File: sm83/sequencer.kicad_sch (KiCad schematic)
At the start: 62 parts

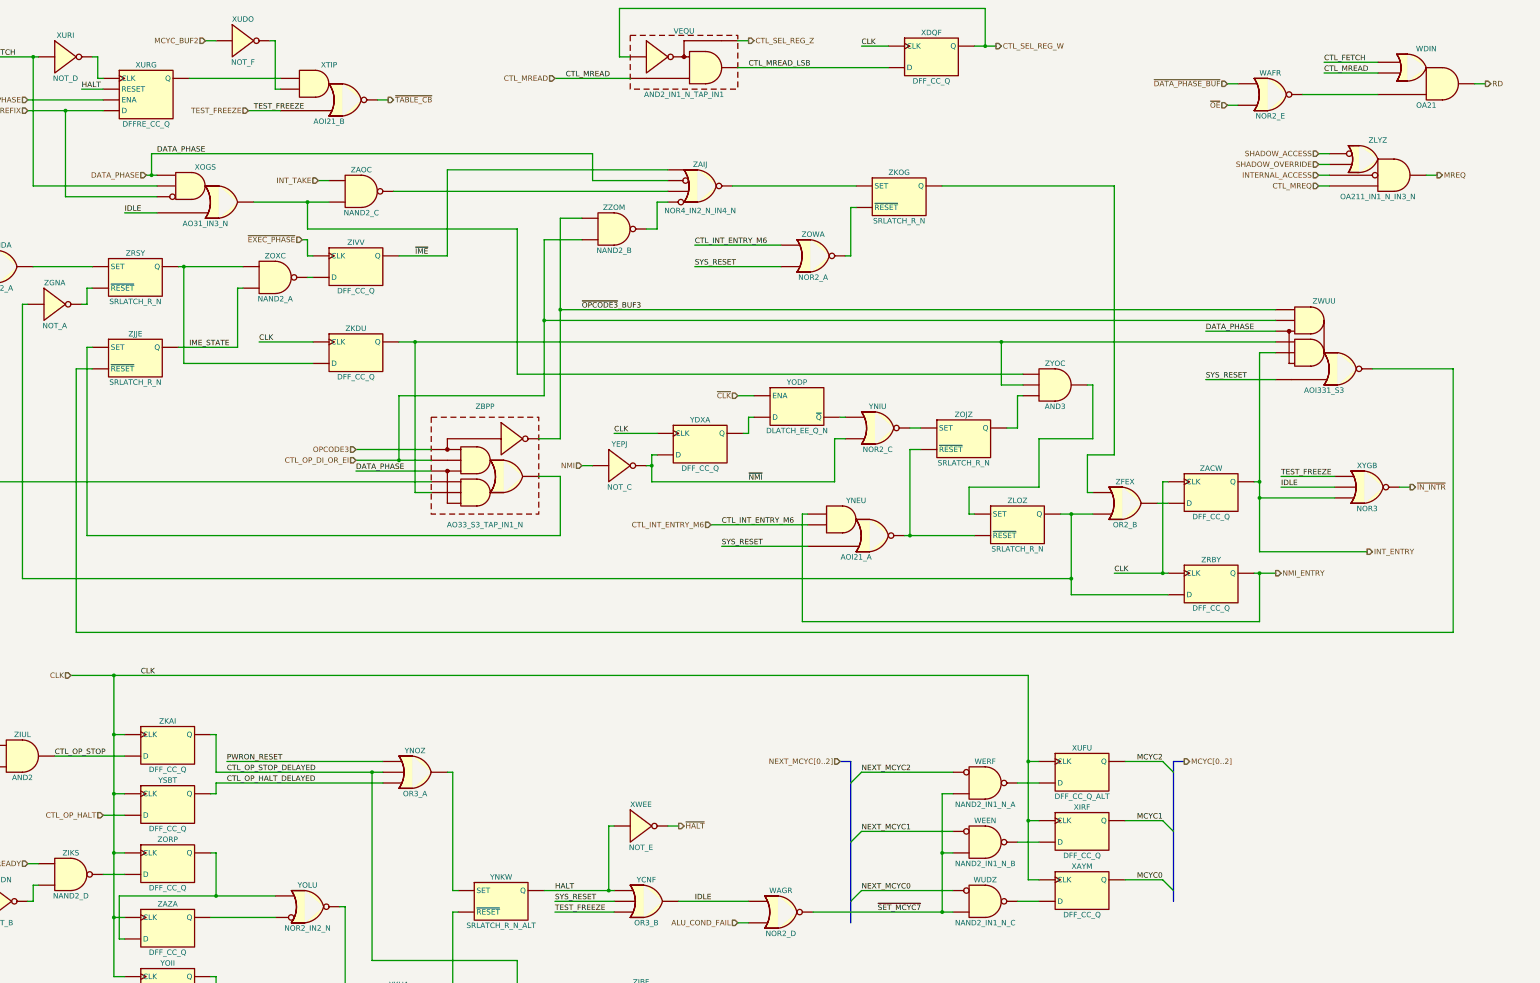
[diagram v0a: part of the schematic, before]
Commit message: SM83: Add decoder1 schematic
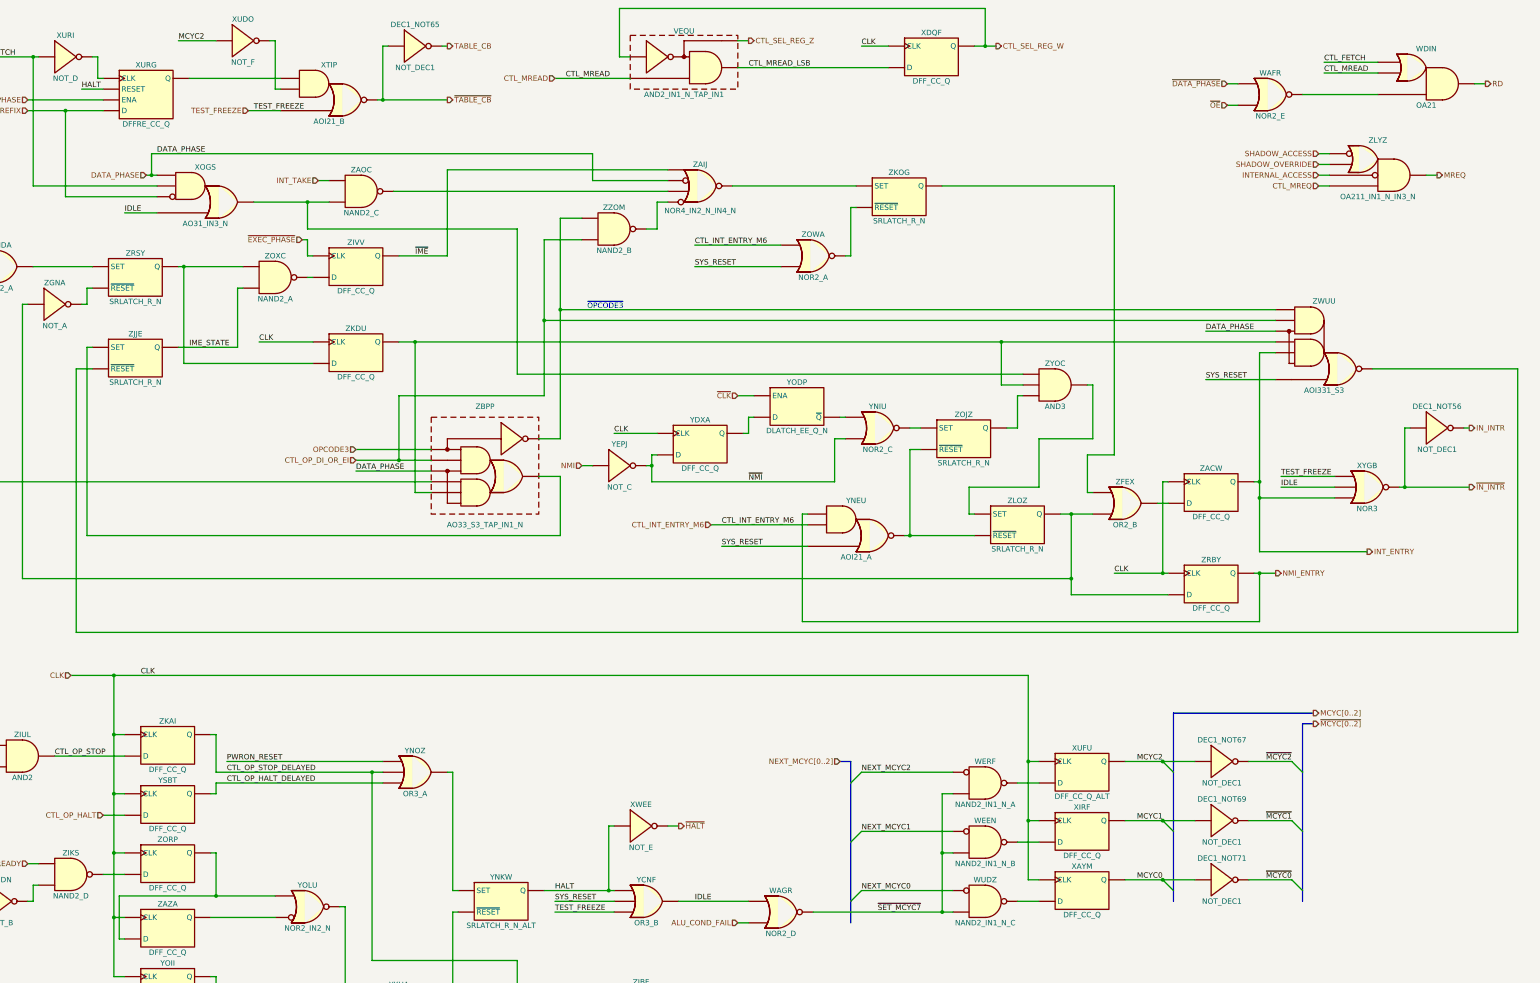
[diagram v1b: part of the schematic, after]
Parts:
- added DEC1_NOT56, DEC1_NOT65, DEC1_NOT67, DEC1_NOT69, DEC1_NOT71: NOT_DEC1, symbol SM83_Cells:NOT_DEC1
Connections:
- net MCYC_BUF2 is gone; now on net MCYC2: XUDO.1
- net MCYC0: now also DEC1_NOT71.1
- net MCYC1: now also DEC1_NOT69.1
- net MCYC2: now also DEC1_NOT67.1
- net ~{IN_INTR}: now also DEC1_NOT56.1
- net ~{TABLE_CB}: now also DEC1_NOT65.1
- net ~{DATA_PHASE_BUF} renamed ~{DATA_PHASE}
- net ~{OPCODE3}_BUF3: no longer names the net of ZBPP. (Y), ZWUU.1, ZZOM.1
- new net: YDXA. (Q), YODP. (~{Q})
- new net: ZKDU. (Q), ZOXC.1, ZRSY. (Q)
- new net: YNEU.4, ZLOZ. (Q), ZOJZ. (Q)
- new net: YOLU.1, ZAZA. (Q), ZORP. (Q)
- new net: ZBPP. (Y), ZJJE. (Q)
- new net IN_INTR: DEC1_NOT56.2
- new net TABLE_CB: DEC1_NOT65.2
- new net ~{MCYC0}: DEC1_NOT71.2
- new net ~{MCYC1}: DEC1_NOT69.2
- new net ~{MCYC2}: DEC1_NOT67.2
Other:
- note added: "~{OPCODE3}"

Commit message: Finish SM83 CPU schematic
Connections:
- new net: YDXA. (Q), YODP. (~{Q})
- new net: ZKDU. (Q), ZOXC.1, ZRSY. (Q)
- new net: YNEU.4, ZLOZ. (Q), ZOJZ. (Q)
- new net: YOLU.1, ZAZA. (Q), ZORP. (Q)
- new net: ZBPP. (Y), ZJJE. (Q)
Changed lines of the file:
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@@
 	(title_block
 		(title "SM83 CPU")
-		(date "2025-12-08")
+		(date "2025-12-24")
 		(rev "0")
 		(company "CC-BY-SA-4.0 Michael Singer")

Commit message: SM83: Merge dist. NANDs and NOR from IRQ_PRIOs
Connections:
- new net: YDXA. (Q), YODP. (~{Q})
- new net: ZKDU. (Q), ZOXC.1, ZRSY. (Q)
- new net: YNEU.4, ZLOZ. (Q), ZOJZ. (Q)
- new net: YOLU.1, ZAZA. (Q), ZORP. (Q)
- new net: ZBPP. (Y), ZJJE. (Q)
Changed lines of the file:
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@@
 	(title_block
 		(title "SM83 CPU")
-		(date "2025-12-24")
+		(date "2025-12-25")
 		(rev "0")
 		(company "CC-BY-SA-4.0 Michael Singer")

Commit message: Release version 0.9 of both schematics
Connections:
- new net: YDXA. (Q), YODP. (~{Q})
- new net: ZKDU. (Q), ZOXC.1, ZRSY. (Q)
- new net: YNEU.4, ZLOZ. (Q), ZOJZ. (Q)
- new net: YOLU.1, ZAZA. (Q), ZORP. (Q)
- new net: ZBPP. (Y), ZJJE. (Q)
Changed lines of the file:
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@@
 		(title "SM83 CPU")
 		(date "2025-12-25")
-		(rev "0")
+		(rev "0.9")
 		(company "CC-BY-SA-4.0 Michael Singer")
 		(comment 1 "https://github.com/msinger/dmg-schematics")

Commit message: Release revision 0.10 of both schematics
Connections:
- new net: YDXA. (Q), YODP. (~{Q})
- new net: ZKDU. (Q), ZOXC.1, ZRSY. (Q)
- new net: YNEU.4, ZLOZ. (Q), ZOJZ. (Q)
- new net: YOLU.1, ZAZA. (Q), ZORP. (Q)
- new net: ZBPP. (Y), ZJJE. (Q)
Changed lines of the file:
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@@
 	(title_block
 		(title "SM83 CPU")
-		(date "2025-12-25")
-		(rev "0.9")
+		(date "2026-03-22")
+		(rev "0.10")
 		(company "CC-BY-SA-4.0 Michael Singer")
 		(comment 1 "https://github.com/msinger/dmg-schematics")
@@
 		)
 		(instances
-			(project ""
+			(project "sm83"
 				(path "/8717d046-1dfd-46fe-a5f7-4e4d2f07de68/bd38470e-a516-485e-8331-c6da5efd6526"
 					(reference "YODP")
@@
 		)
 		(instances
-			(project ""
+			(project "sm83"
 				(path "/8717d046-1dfd-46fe-a5f7-4e4d2f07de68/bd38470e-a516-485e-8331-c6da5efd6526"
 					(reference "WAGR")
@@
 		)
 		(instances
-			(project ""
+			(project "sm83"
 				(path "/8717d046-1dfd-46fe-a5f7-4e4d2f07de68/bd38470e-a516-485e-8331-c6da5efd6526"
 					(reference "YCNF")
@@
 		)
 		(instances
-			(project ""
+			(project "sm83"
 				(path "/8717d046-1dfd-46fe-a5f7-4e4d2f07de68/bd38470e-a516-485e-8331-c6da5efd6526"
 					(reference "ZWLM")
@@
 		)
 		(instances
-			(project ""
+			(project "sm83"
 				(path "/8717d046-1dfd-46fe-a5f7-4e4d2f07de68/bd38470e-a516-485e-8331-c6da5efd6526"
 					(reference "ZYOC")
@@
 		)
 		(instances
-			(project ""
+			(project "sm83"
 				(path "/8717d046-1dfd-46fe-a5f7-4e4d2f07de68/bd38470e-a516-485e-8331-c6da5efd6526"
 					(reference "ZWUU")
@@
 		)
 		(instances
-			(project ""
+			(project "sm83"
 				(path "/8717d046-1dfd-46fe-a5f7-4e4d2f07de68/bd38470e-a516-485e-8331-c6da5efd6526"
 					(reference "ZAOC")
@@
 		)
 		(instances
-			(project ""
+			(project "sm83"
 				(path "/8717d046-1dfd-46fe-a5f7-4e4d2f07de68/bd38470e-a516-485e-8331-c6da5efd6526"
 					(reference "YOLU")
@@
 		)
 		(instances
-			(project ""
+			(project "sm83"
 				(path "/8717d046-1dfd-46fe-a5f7-4e4d2f07de68/bd38470e-a516-485e-8331-c6da5efd6526"
 					(reference "ZIUL")
@@
 		)
 		(instances
-			(project ""
+			(project "sm83"
 				(path "/8717d046-1dfd-46fe-a5f7-4e4d2f07de68/bd38470e-a516-485e-8331-c6da5efd6526"
 					(reference "XURI")
@@
 		)
 		(instances
-			(project ""
+			(project "sm83"
 				(path "/8717d046-1dfd-46fe-a5f7-4e4d2f07de68/bd38470e-a516-485e-8331-c6da5efd6526"
 					(reference "WAFR")
@@
 		)
 		(instances
-			(project ""
+			(project "sm83"
 				(path "/8717d046-1dfd-46fe-a5f7-4e4d2f07de68/bd38470e-a516-485e-8331-c6da5efd6526"
 					(reference "YNEU")
@@
 		)
 		(instances
-			(project ""
+			(project "sm83"
 				(path "/8717d046-1dfd-46fe-a5f7-4e4d2f07de68/bd38470e-a516-485e-8331-c6da5efd6526"
 					(reference "ZOWA")
@@
 		)
 		(instances
-			(project ""
+			(project "sm83"
 				(path "/8717d046-1dfd-46fe-a5f7-4e4d2f07de68/bd38470e-a516-485e-8331-c6da5efd6526"
 					(reference "WEEN")
@@
 		)
 		(instances
-			(project ""
+			(project "sm83"
 				(path "/8717d046-1dfd-46fe-a5f7-4e4d2f07de68/bd38470e-a516-485e-8331-c6da5efd6526"
 					(reference "XWEE")
@@
 		)
 		(instances
-			(project ""
+			(project "sm83"
 				(path "/8717d046-1dfd-46fe-a5f7-4e4d2f07de68/bd38470e-a516-485e-8331-c6da5efd6526"
 					(reference "ZJBF")
@@
 		)
 		(instances
-			(project ""
+			(project "sm83"
 				(path "/8717d046-1dfd-46fe-a5f7-4e4d2f07de68/bd38470e-a516-485e-8331-c6da5efd6526"
 					(reference "ZFEX")
@@
 		)
 		(instances
-			(project ""
+			(project "sm83"
 				(path "/8717d046-1dfd-46fe-a5f7-4e4d2f07de68/bd38470e-a516-485e-8331-c6da5efd6526"
 					(reference "XUFU")
@@
 		)
 		(instances
-			(project ""
+			(project "sm83"
 				(path "/8717d046-1dfd-46fe-a5f7-4e4d2f07de68/bd38470e-a516-485e-8331-c6da5efd6526"
 					(reference "ZUDN")
@@
 		)
 		(instances
-			(project ""
+			(project "sm83"
 				(path "/8717d046-1dfd-46fe-a5f7-4e4d2f07de68/bd38470e-a516-485e-8331-c6da5efd6526"
 					(reference "WERF")
@@
 		)
 		(instances
-			(project ""
+			(project "sm83"
 				(path "/8717d046-1dfd-46fe-a5f7-4e4d2f07de68/bd38470e-a516-485e-8331-c6da5efd6526"
 					(reference "ZGNA")
@@
 		)
 		(instances
-			(project ""
+			(project "sm83"
 				(path "/8717d046-1dfd-46fe-a5f7-4e4d2f07de68/bd38470e-a516-485e-8331-c6da5efd6526"
 					(reference "WUDZ")
@@
 		)
 		(instances
-			(project ""
+			(project "sm83"
 				(path "/8717d046-1dfd-46fe-a5f7-4e4d2f07de68/bd38470e-a516-485e-8331-c6da5efd6526"
 					(reference "XIRF")
@@
 		)
 		(instances
-			(project ""
+			(project "sm83"
 				(path "/8717d046-1dfd-46fe-a5f7-4e4d2f07de68/bd38470e-a516-485e-8331-c6da5efd6526"
 					(reference "XUDO")
@@
 		)
 		(instances
-			(project ""
+			(project "sm83"
 				(path "/8717d046-1dfd-46fe-a5f7-4e4d2f07de68/bd38470e-a516-485e-8331-c6da5efd6526"
 					(reference "ZBPP")
@@
 		)
 		(instances
-			(project ""
+			(project "sm83"
 				(path "/8717d046-1dfd-46fe-a5f7-4e4d2f07de68/bd38470e-a516-485e-8331-c6da5efd6526"
 					(reference "ZOXC")
@@
 		)
 		(instances
-			(project ""
+			(project "sm83"
 				(path "/8717d046-1dfd-46fe-a5f7-4e4d2f07de68/bd38470e-a516-485e-8331-c6da5efd6526"
 					(reference "ZHZO")
@@
 		)
 		(instances
-			(project ""
+			(project "sm83"
 				(path "/8717d046-1dfd-46fe-a5f7-4e4d2f07de68/bd38470e-a516-485e-8331-c6da5efd6526"
 					(reference "YNOZ")
@@
 		)
 		(instances
-			(project ""
+			(project "sm83"
 				(path "/8717d046-1dfd-46fe-a5f7-4e4d2f07de68/bd38470e-a516-485e-8331-c6da5efd6526"
 					(reference "ZUMN")
@@
 		)
 		(instances
-			(project ""
+			(project "sm83"
 				(path "/8717d046-1dfd-46fe-a5f7-4e4d2f07de68/bd38470e-a516-485e-8331-c6da5efd6526"
 					(reference "XAYM")
@@
 		)
 		(instances
-			(project ""
+			(project "sm83"
 				(path "/8717d046-1dfd-46fe-a5f7-4e4d2f07de68/bd38470e-a516-485e-8331-c6da5efd6526"
 					(reference "XOGS")
@@
 		)
 		(instances
-			(project ""
+			(project "sm83"
 				(path "/8717d046-1dfd-46fe-a5f7-4e4d2f07de68/bd38470e-a516-485e-8331-c6da5efd6526"
 					(reference "ZKON")
@@
 		)
 		(instances
-			(project ""
+			(project "sm83"
 				(path "/8717d046-1dfd-46fe-a5f7-4e4d2f07de68/bd38470e-a516-485e-8331-c6da5efd6526"
 					(reference "YEPJ")
@@
 		)
 		(instances
-			(project ""
+			(project "sm83"
 				(path "/8717d046-1dfd-46fe-a5f7-4e4d2f07de68/bd38470e-a516-485e-8331-c6da5efd6526"
 					(reference "XURG")
@@
 		)
 		(instances
-			(project ""
+			(project "sm83"
 				(path "/8717d046-1dfd-46fe-a5f7-4e4d2f07de68/bd38470e-a516-485e-8331-c6da5efd6526"
 					(reference "YNKW")
@@
 		)
 		(instances
-			(project ""
+			(project "sm83"
 				(path "/8717d046-1dfd-46fe-a5f7-4e4d2f07de68/bd38470e-a516-485e-8331-c6da5efd6526"
 					(reference "YNIU")
@@
 		)
 		(instances
-			(project ""
+			(project "sm83"
 				(path "/8717d046-1dfd-46fe-a5f7-4e4d2f07de68/bd38470e-a516-485e-8331-c6da5efd6526"
 					(reference "YKUA")
@@
 		)
 		(instances
-			(project ""
+			(project "sm83"
 				(path "/8717d046-1dfd-46fe-a5f7-4e4d2f07de68/bd38470e-a516-485e-8331-c6da5efd6526"
 					(reference "WDIN")
@@
 		)
 		(instances
-			(project ""
+			(project "sm83"
 				(path "/8717d046-1dfd-46fe-a5f7-4e4d2f07de68/bd38470e-a516-485e-8331-c6da5efd6526"
 					(reference "DEC1_NOT67")
@@
 		)
 		(instances
-			(project ""
+			(project "sm83"
 				(path "/8717d046-1dfd-46fe-a5f7-4e4d2f07de68/bd38470e-a516-485e-8331-c6da5efd6526"
 					(reference "XTIP")
@@
 		)
 		(instances
-			(project ""
+			(project "sm83"
 				(path "/8717d046-1dfd-46fe-a5f7-4e4d2f07de68/bd38470e-a516-485e-8331-c6da5efd6526"
 					(reference "ZLYZ")
@@
 		)
 		(instances
-			(project ""
+			(project "sm83"
 				(path "/8717d046-1dfd-46fe-a5f7-4e4d2f07de68/bd38470e-a516-485e-8331-c6da5efd6526"
 					(reference "ZNDA")
@@
 		)
 		(instances
-			(project ""
+			(project "sm83"
 				(path "/8717d046-1dfd-46fe-a5f7-4e4d2f07de68/bd38470e-a516-485e-8331-c6da5efd6526"
 					(reference "ZAIJ")
@@
 		)
 		(instances
-			(project ""
+			(project "sm83"
 				(path "/8717d046-1dfd-46fe-a5f7-4e4d2f07de68/bd38470e-a516-485e-8331-c6da5efd6526"
 					(reference "ZZOM")
@@
 		)
 		(instances
-			(project ""
+			(project "sm83"
 				(path "/8717d046-1dfd-46fe-a5f7-4e4d2f07de68/bd38470e-a516-485e-8331-c6da5efd6526"
 					(reference "VEQU")
@@
 		)
 		(instances
-			(project ""
+			(project "sm83"
 				(path "/8717d046-1dfd-46fe-a5f7-4e4d2f07de68/bd38470e-a516-485e-8331-c6da5efd6526"
 					(reference "ZIKS")
@@
 		)
 		(instances
-			(project ""
+			(project "sm83"
 				(path "/8717d046-1dfd-46fe-a5f7-4e4d2f07de68/bd38470e-a516-485e-8331-c6da5efd6526"
 					(reference "XYGB")

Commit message: Release revision 0.11 of both schematics
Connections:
- new net: YDXA. (Q), YODP. (~{Q})
- new net: ZKDU. (Q), ZOXC.1, ZRSY. (Q)
- new net: YNEU.4, ZLOZ. (Q), ZOJZ. (Q)
- new net: YOLU.1, ZAZA. (Q), ZORP. (Q)
- new net: ZBPP. (Y), ZJJE. (Q)
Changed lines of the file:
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@@
 	(title_block
 		(title "SM83 CPU")
-		(date "2026-03-22")
-		(rev "0.10")
+		(date "2026-04-11")
+		(rev "0.11")
 		(company "CC-BY-SA-4.0 Michael Singer")
 		(comment 1 "https://github.com/msinger/dmg-schematics")
